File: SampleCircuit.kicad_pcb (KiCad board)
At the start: 2 copper layers, 100 x 90 mm, 65 parts, among them J1 24V INPUT, J2 12V TEST, J3 5V TEST, J4 3.3V TEST, J5 SPEAKER, SW1 RESET, SW2 BOOT, U1 LMZM23601SILR, U15 TLV803S, U2 ESP32-S3-WROOM-1, U23 RV-3028-C7, U24 LMZM23601SILR, U25 LMZM23601SILR, U5 NS4168, U6 MicroSD

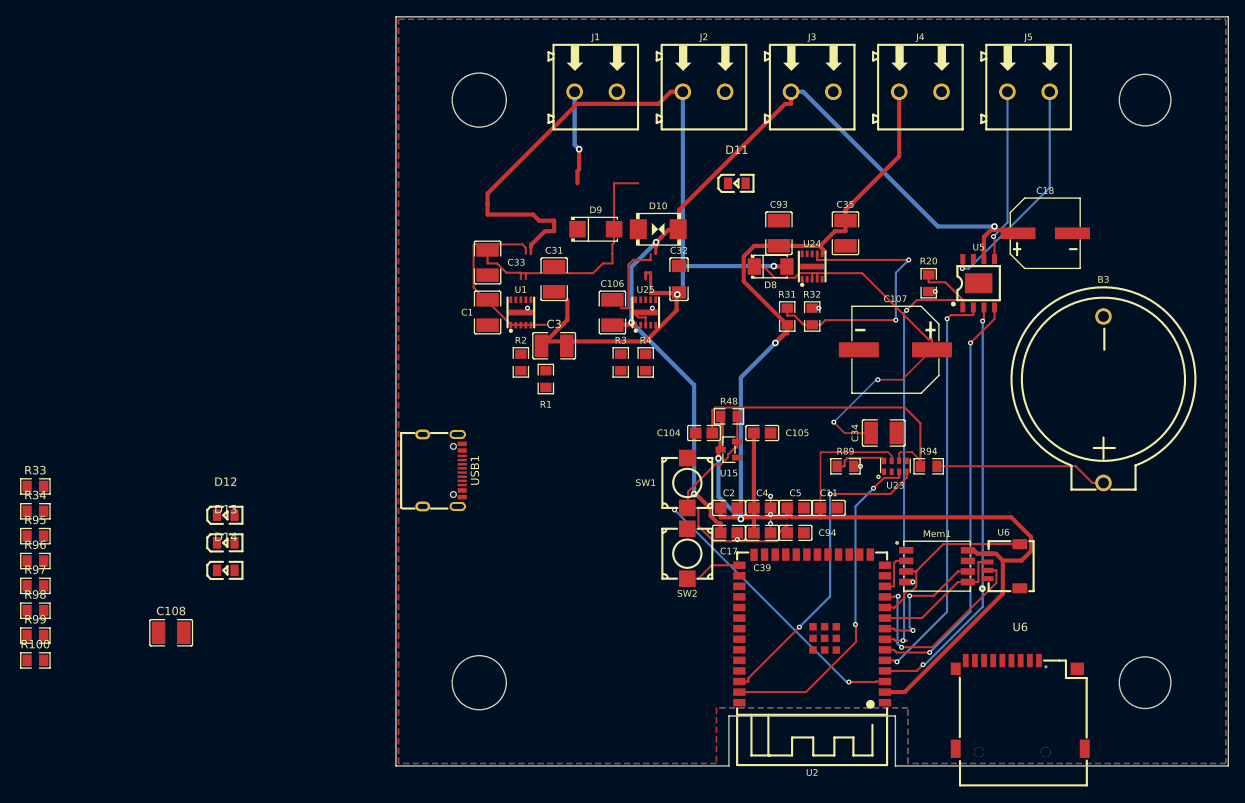
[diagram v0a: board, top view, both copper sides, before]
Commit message: Remove stray Molex SD card footprint, remove all traces/vias for re-routing
Co-Authored-By: Claude Opus 4.6 (1M context) <noreply@anthropic.com>
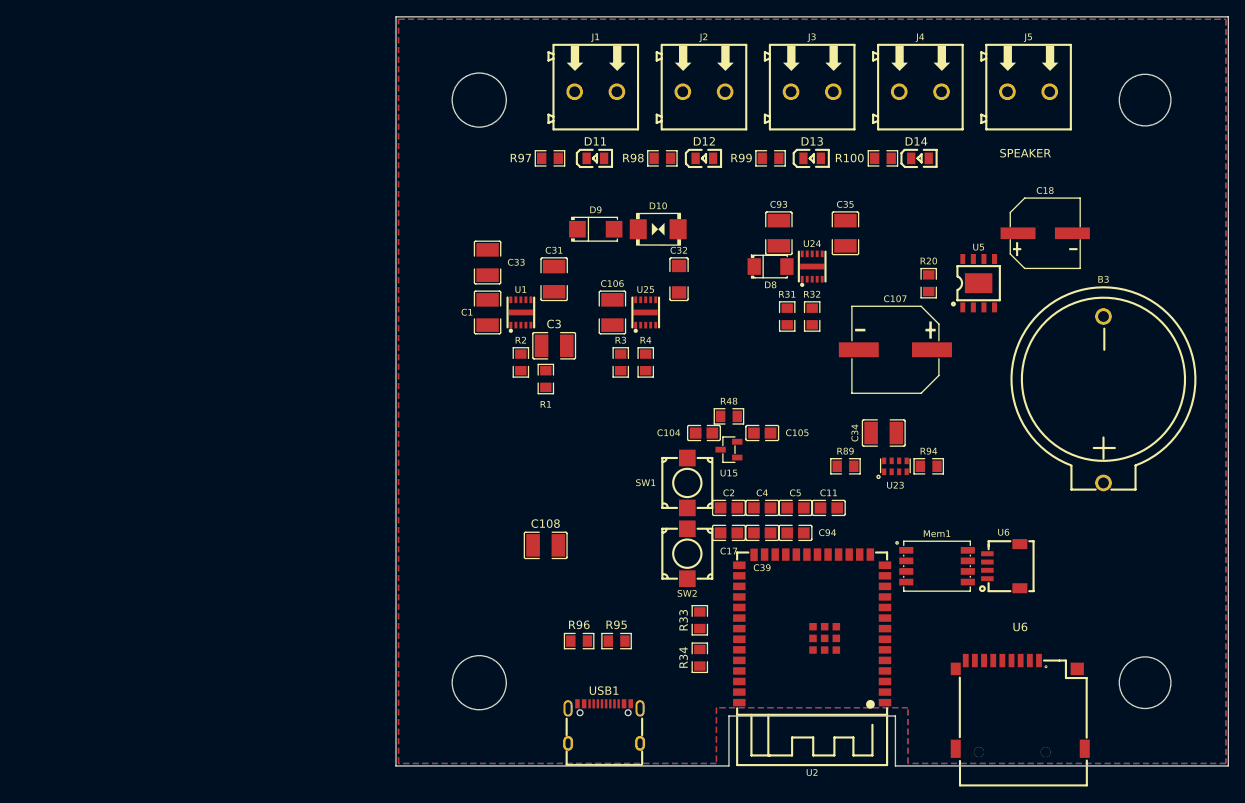
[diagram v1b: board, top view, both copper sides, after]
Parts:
- moved R100 118.4 mm to (158.5, 63.0)
- moved R99 105.3 mm to (145.0, 63.0)
- moved D14 97.0 mm to (162.9, 63.0)
- moved R98 92.9 mm to (132.0, 63.0)
- moved D13 84.2 mm to (150.0, 63.0)
- moved R34 81.7 mm to (136.5, 123.0), turned to 90 degrees
- moved R33 81.4 mm to (136.5, 118.5), turned to 90 degrees
- moved R97 80.4 mm to (118.5, 63.0)
- moved D12 71.7 mm to (137.1, 63.0)
- moved R95 71.0 mm to (126.5, 121.0)
- moved R96 66.0 mm to (122.0, 121.0)
- moved C108 46.2 mm to (118.0, 109.5)
- moved USB1 36.1 mm to (125.0, 130.9), turned to 0 degrees
- moved D11 17.3 mm to (124.0, 63.0)
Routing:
- net +3.3V: track 193.2 -> 0.00 mm, vias 3 -> 0
- net +12V: track 114.6 -> 0.00 mm, vias 2 -> 0
- net +5V: track 108.5 -> 0.00 mm, vias 4 -> 0
- net Enable: track 67.0 -> 0.00 mm, vias 2 -> 0
- net AMP_EN: track 57.2 -> 0.00 mm, vias 2 -> 0
- net BCLK: track 51.0 -> 0.00 mm, vias 2 -> 0
- net DIN: track 50.2 -> 0.00 mm, vias 2 -> 0
- net LRCLK: track 49.5 -> 0.00 mm, vias 2 -> 0
- net Net-(D8-K): track 48.6 -> 0.00 mm, vias 2 -> 0
- net SCL: track 40.2 -> 0.00 mm, vias 2 -> 0
- net Net-(U23-VBACKUP): track 38.4 -> 0.00 mm
- net SDA: track 38.4 -> 0.00 mm, vias 2 -> 0
- net Net-(U24-FB): track 34.2 -> 0.00 mm, vias 2 -> 0
- net Net-(D10-K): track 31.2 -> 0.00 mm
- net OUTP: track 27.2 -> 0.00 mm, vias 1 -> 0
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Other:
- board text added: "SPEAKER"

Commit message: Autoroute PCB with FreeRouting, fix GND zone thermals and edge clearance
- Swap discontinued 100k resistor C17407 to Basic C149504 (schematic + PCB)
- Set GND zone thermal relief to 0.5mm spoke/gap per spec
- Pull copper pour 1mm from board edge (was 0.3mm) per spec 18h
- Autoroute all nets via FreeRouting (2 manually completed near U23 RTC)
- DRC clean: 0 unconnected, 0 shorts, 3 non-critical warnings remaining

Co-Authored-By: Claude Opus 4.6 (1M context) <noreply@anthropic.com>
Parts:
- removed the U6 at (173.0, 112.0)
- moved C1 5.52 mm to (111.0, 76.0)
- moved C106 5.52 mm to (126.0, 76.0)
- moved C3 5.52 mm to (119.0, 80.0)
- moved C31 5.52 mm to (119.0, 72.0)
- moved C32 5.52 mm to (134.0, 72.0)
- moved C33 5.52 mm to (111.0, 70.0)
- moved D10 5.52 mm to (131.5, 66.0)
- moved D9 5.52 mm to (124.0, 66.0)
- moved R1 5.52 mm to (118.0, 84.0)
- moved R2 5.52 mm to (115.0, 82.0)
- moved R3 5.52 mm to (127.0, 82.0)
- moved R4 5.52 mm to (130.0, 82.0)
- moved U1 5.52 mm to (115.0, 76.0)
- moved U25 5.52 mm to (130.0, 76.0)
- moved C34 1.71 mm to (160.0, 95.0), turned to 90 degrees
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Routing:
- net GND: track 0.00 -> 667.9 mm, vias 0 -> 2
- net +3.3V: track 0.00 -> 280.0 mm, vias 0 -> 13
- net +5V: track 0.00 -> 174.9 mm, vias 0 -> 5
- net +12V: track 0.00 -> 134.1 mm, vias 0 -> 7
- net Net-(D8-K): track 0.00 -> 108.0 mm, vias 0 -> 2
- net DIN: track 0.00 -> 57.8 mm, vias 0 -> 2
- net Enable: track 0.00 -> 57.7 mm, vias 0 -> 2
- net SCL: track 0.00 -> 55.0 mm, vias 0 -> 2
- net AMP_EN: track 0.00 -> 54.4 mm, vias 0 -> 2
- net UD+: track 0.00 -> 54.3 mm, vias 0 -> 2
- net Net-(D10-K): track 0.00 -> 51.8 mm
- net BCLK: track 0.00 -> 51.2 mm, vias 0 -> 2
- net LRCLK: track 0.00 -> 50.6 mm, vias 0 -> 2
- net SDA: track 0.00 -> 48.4 mm, vias 0 -> 2
- net SD_CLK: track 0.00 -> 43.6 mm, vias 0 -> 2
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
